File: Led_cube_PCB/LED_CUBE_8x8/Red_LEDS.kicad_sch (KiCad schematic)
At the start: 34 parts, among them IC16 74AHCT244PW,118, IC19 74AHCT244PW,118, IC20 74AHCT244PW,118, IC21 74AHCT244PW,118, IC22 74AHCT244PW,118, IC4 74AHCT244PW,118, IC5 74AHCT244PW,118, IC6 74AHCT244PW,118, IC7 74AHC138PW,118

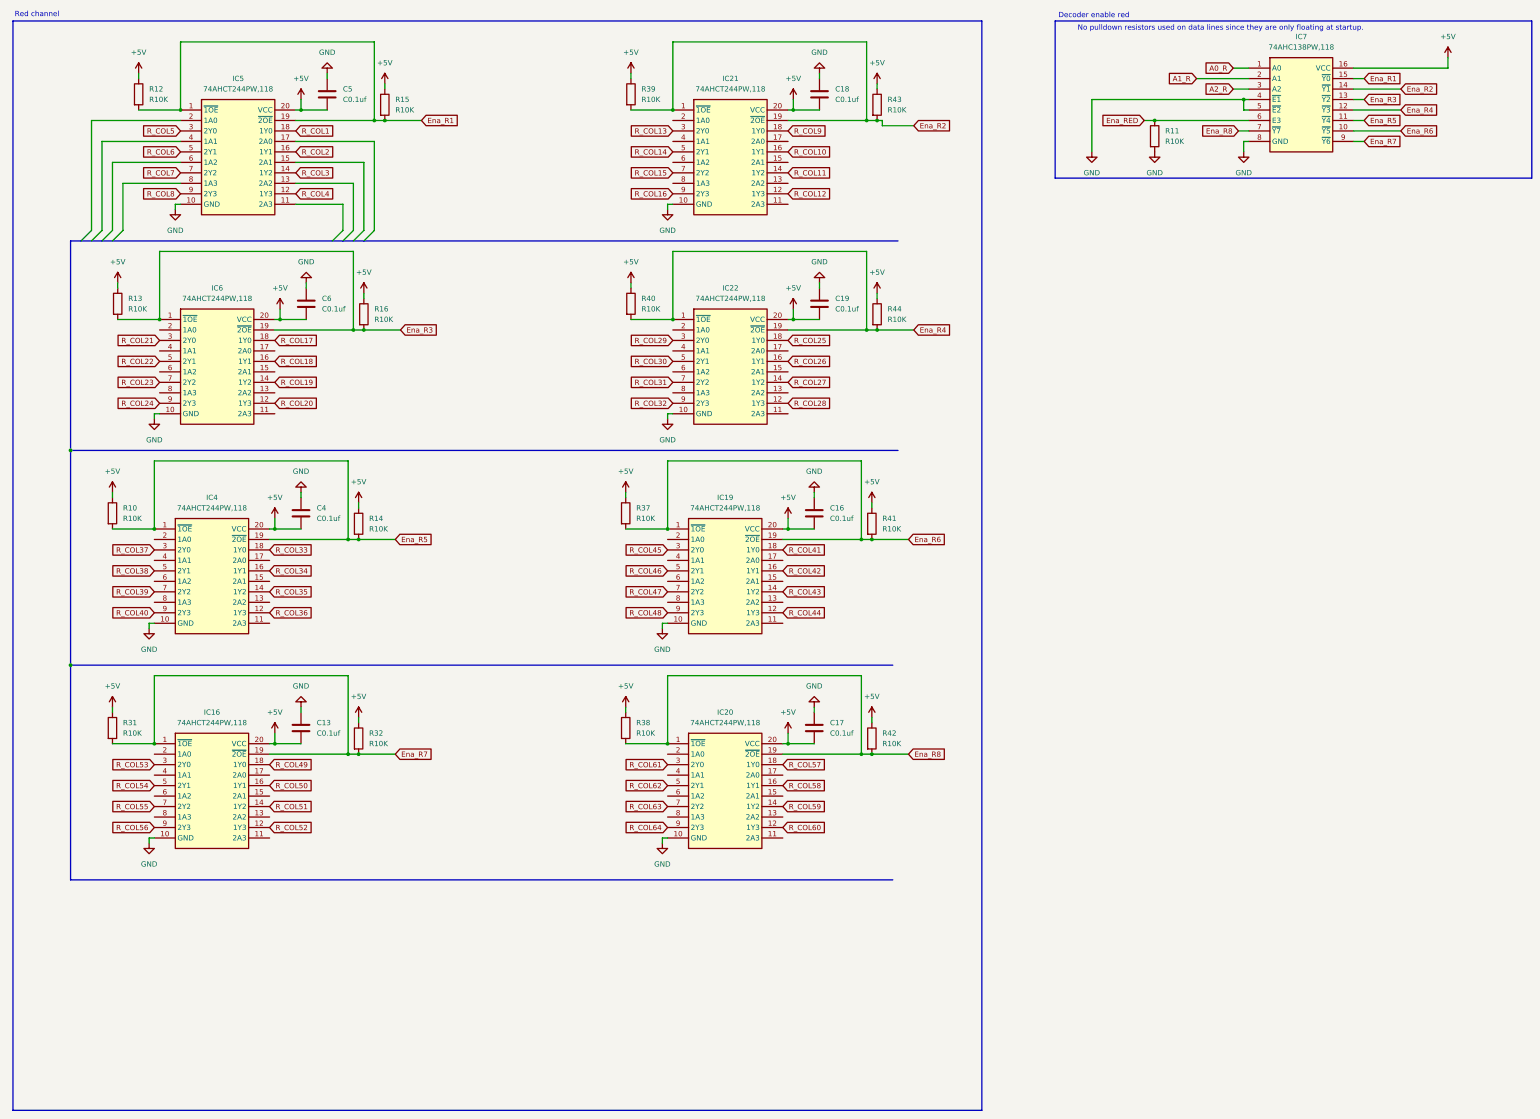
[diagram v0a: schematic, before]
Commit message: Finished the schematic for the red green and blue color multiplexing.
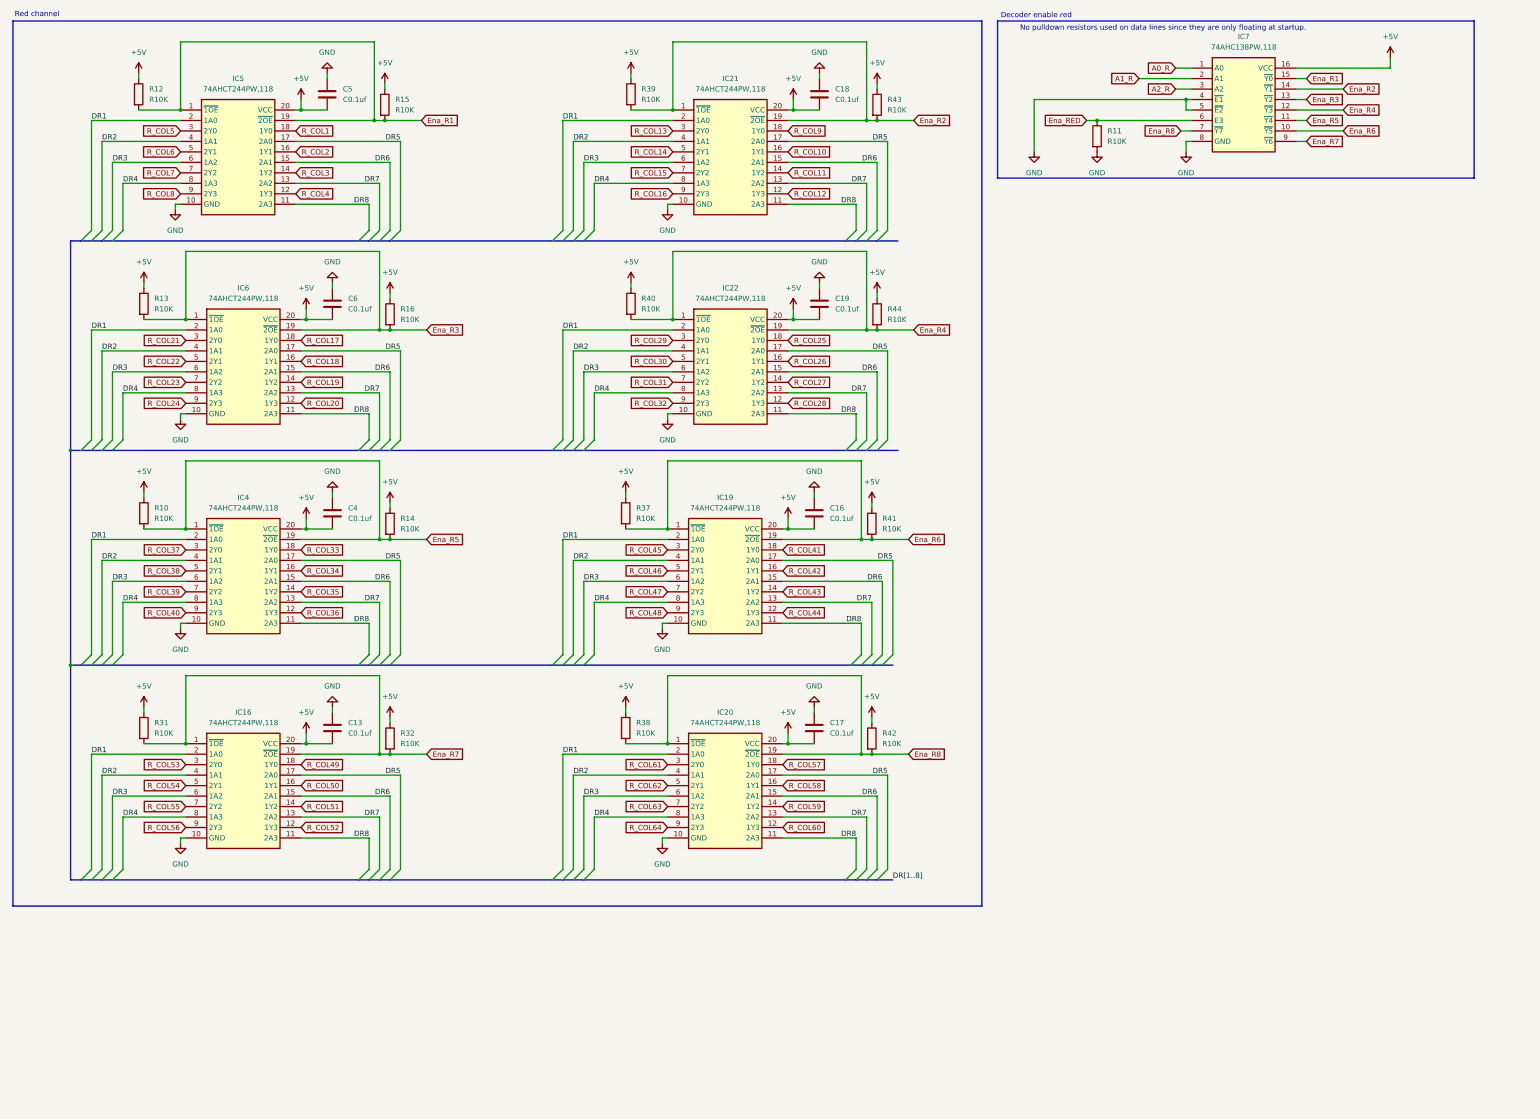
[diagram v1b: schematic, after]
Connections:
- net DR8: now reaches IC21.11 (2A3)
- net DR8: now also IC16.11 (2A3), IC19.11 (2A3), IC20.11 (2A3), IC22.11 (2A3), IC4.11 (2A3), IC5.11 (2A3), IC6.11 (2A3)
- net DR7: now reaches IC21.13 (2A2)
- net DR7: now also IC16.13 (2A2), IC19.13 (2A2), IC20.13 (2A2), IC22.13 (2A2), IC4.13 (2A2), IC5.13 (2A2), IC6.13 (2A2)
- net DR6: now reaches IC21.15 (2A1)
- net DR6: now also IC16.15 (2A1), IC19.15 (2A1), IC20.15 (2A1), IC22.15 (2A1), IC4.15 (2A1), IC5.15 (2A1), IC6.15 (2A1)
- net DR5: now reaches IC21.17 (2A0)
- net DR5: now also IC16.17 (2A0), IC19.17 (2A0), IC20.17 (2A0), IC22.17 (2A0), IC4.17 (2A0), IC5.17 (2A0), IC6.17 (2A0)
- net DR1: now reaches IC21.2 (1A0)
- net DR1: now also IC16.2 (1A0), IC19.2 (1A0), IC20.2 (1A0), IC22.2 (1A0), IC4.2 (1A0), IC5.2 (1A0), IC6.2 (1A0)
- net DR2: now reaches IC21.4 (1A1)
- net DR2: now also IC16.4 (1A1), IC19.4 (1A1), IC20.4 (1A1), IC22.4 (1A1), IC4.4 (1A1), IC5.4 (1A1), IC6.4 (1A1)
- net DR3: now reaches IC21.6 (1A2)
- net DR3: now also IC16.6 (1A2), IC19.6 (1A2), IC20.6 (1A2), IC22.6 (1A2), IC4.6 (1A2), IC5.6 (1A2), IC6.6 (1A2)
- net DR4: now reaches IC21.8 (1A3)
- net DR4: now also IC16.8 (1A3), IC19.8 (1A3), IC20.8 (1A3), IC22.8 (1A3), IC4.8 (1A3), IC5.8 (1A3), IC6.8 (1A3)
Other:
- company: (none) -> Áuthor: Lars Molenschot
- title: Red LED's -> 8x8_Led_Cube
- moved on the sheet: C13, C4, C6, IC16, IC4, IC6, IC7, R10, R11, R13, R14, R16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

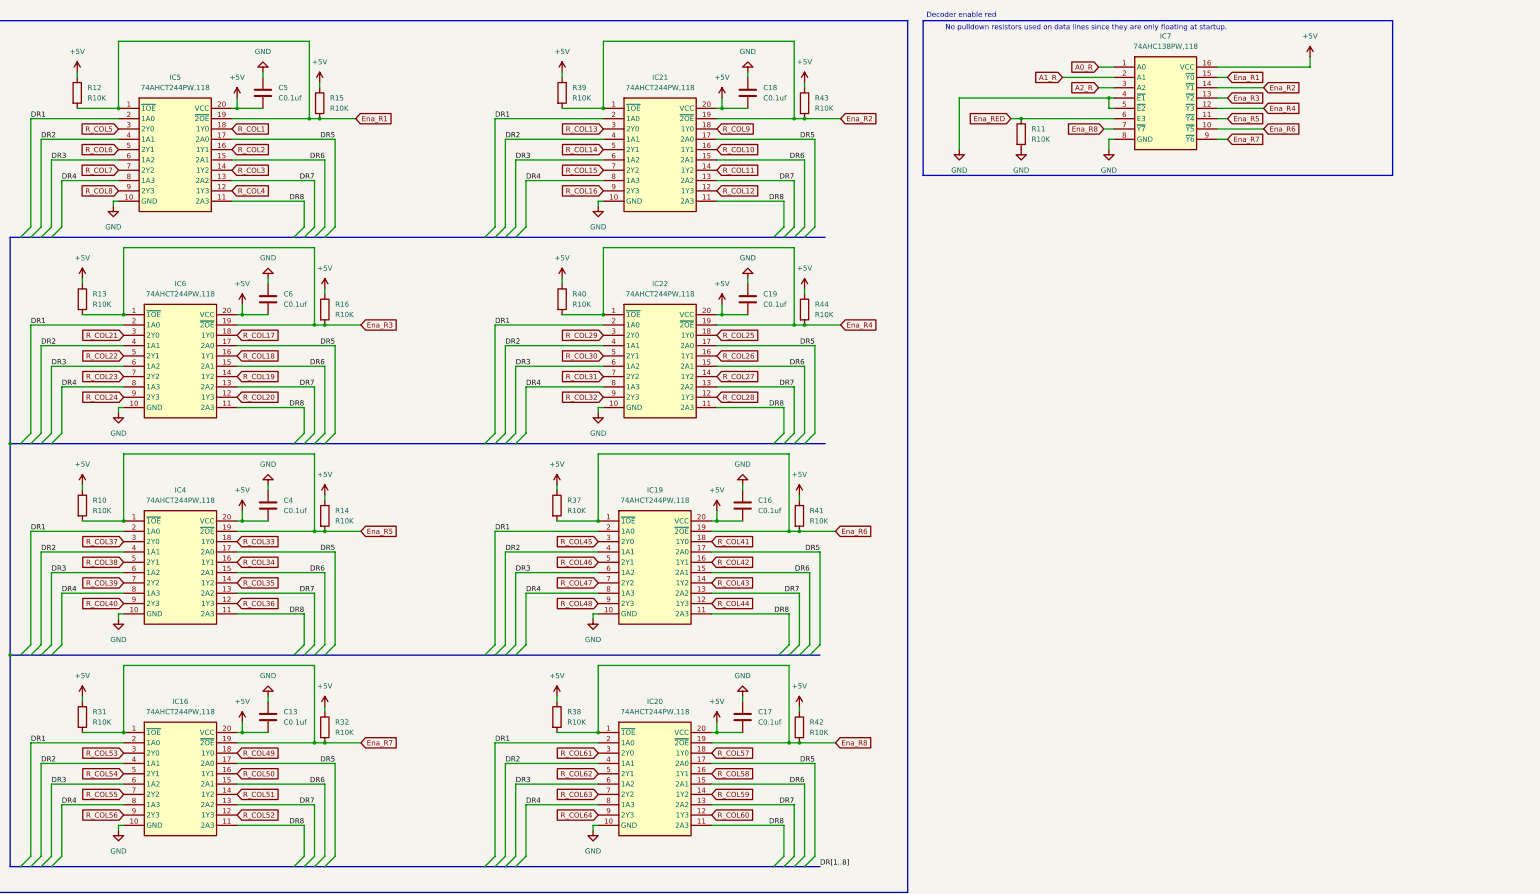
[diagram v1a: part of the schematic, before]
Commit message: added power schematic and updated labels to correct type e.g. output, input
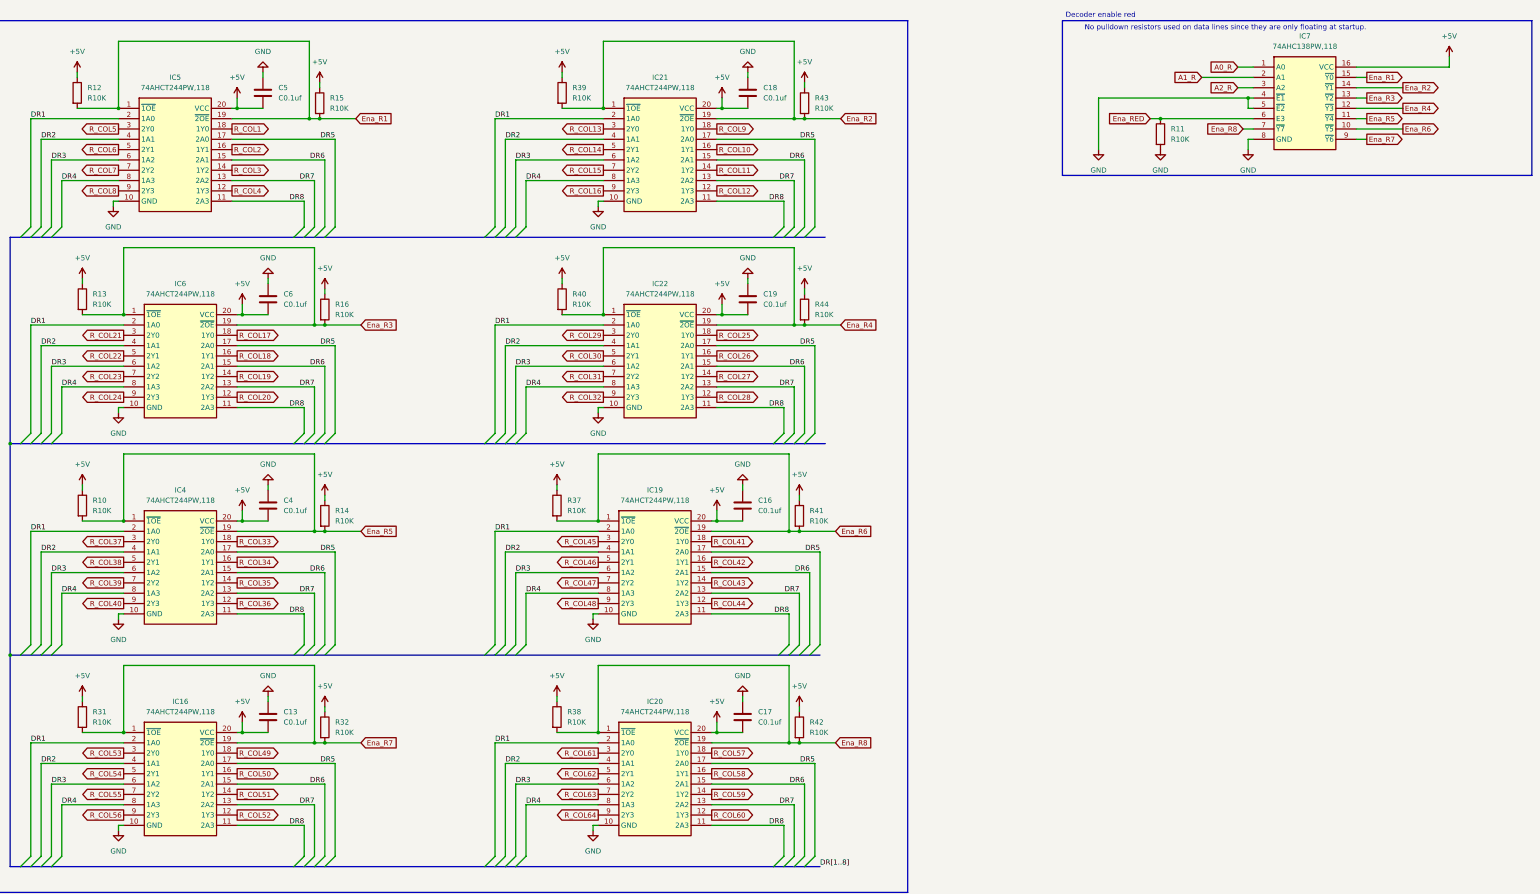
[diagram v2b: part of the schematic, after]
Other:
- moved on the sheet: IC7, R11
